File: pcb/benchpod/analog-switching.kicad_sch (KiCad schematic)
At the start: 8 parts, among them U53 TPL7407LAPWR, U58 TCA9554PWR

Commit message: fix pull-downs for board boot-up
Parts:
- added R170, R171, R172, R173: 4.7k, Resistor_SMD:R_0402_1005Metric, symbol Device:R
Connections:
- net AMP_MEASURE: now also R172.1
- net CAL1: now also R170.1
- net CAL2: now also R171.1
- net CAL_PATH: now also R173.1
- net GND: now also R170.2, R171.2, R172.2, R173.2
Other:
- moved on the sheet: C210, C211, C227, C229, FB8, R161, U53, U58

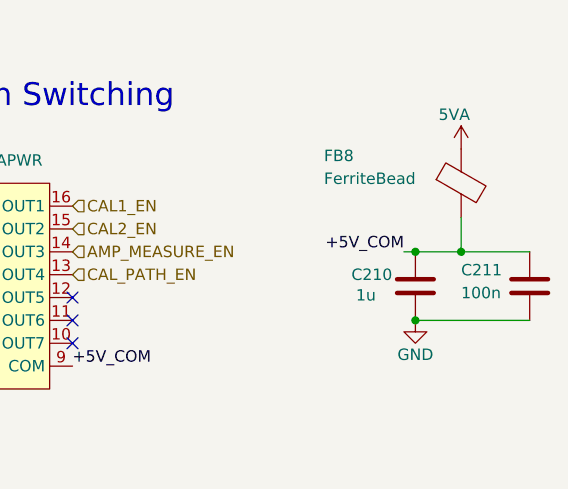
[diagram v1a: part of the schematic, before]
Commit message: 5VA->5V for relays, resistor and cap changes
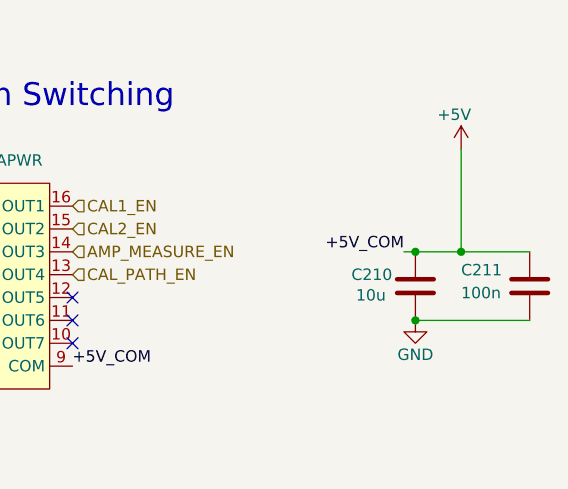
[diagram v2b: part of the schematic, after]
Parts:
- removed FB8: FerriteBead, lcsc:L0603, symbol Device:FerriteBead
- C210: value 1u -> 10u; footprint Capacitor_SMD:C_0402_1005Metric -> Capacitor_SMD:C_0603_1608Metric; LCSC C1518208 -> C96446
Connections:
- net +5V_COM renamed +5V
